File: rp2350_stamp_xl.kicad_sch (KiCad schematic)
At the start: 47 parts, among them J1 Conn_North, J2 Conn_West, J3 Conn_East, J4 Conn_South, J5 Conn_Pi_SWD, J6 Conn_Pi_UART, Q1 BSS84, SW1 SW_RESET, SW2 SW_BOOTSEL, U1 W25Q128JVPIQ, U2 ME4055, U3 AP2112K-3.3, U4 FLASH or PSRAM, U5 RP235x-B, Y1 XYDBPCNANF-12MHZ

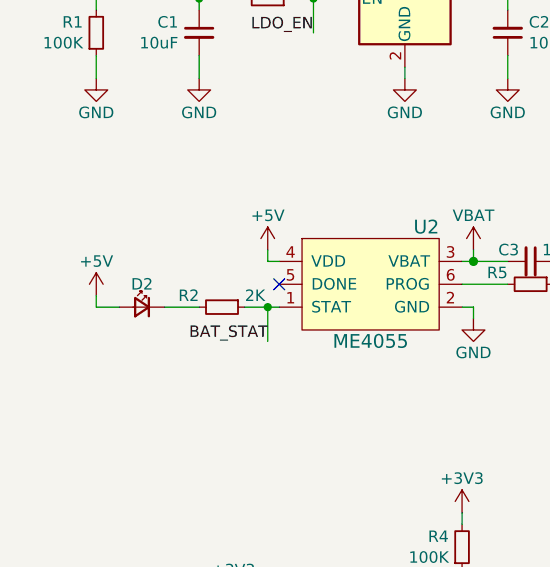
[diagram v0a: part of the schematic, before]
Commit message: Rev 3
- Rev 2 added logo and QR Code
- Put chip name on the board
- Fixup pin markers to be uniform
- Add battery icon
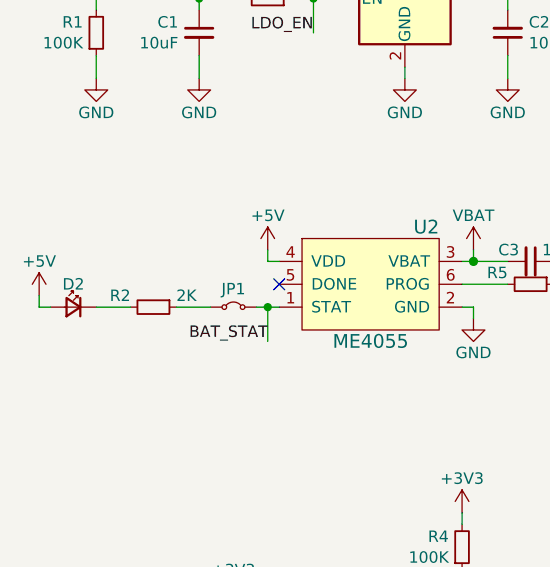
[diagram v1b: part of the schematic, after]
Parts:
- added JP1: SJ_STAT_LED, Jumper:SolderJumper-2_P1.3mm_Bridged_RoundedPad1.0x1.5mm, symbol Jumper:Jumper_2_Small_Bridged
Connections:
- net BAT_STAT: now also JP1.2 (B); no longer R2.1
- new net: JP1.1 (A), R2.1
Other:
- moved on the sheet: D2, R2
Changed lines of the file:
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@@
 	(wire
 		(pts
+			(xy 44.45 96.52) (xy 45.72 96.52)
+		)
+		(stroke
+			(width 0)
+			(type default)
+		)
+	)
+	(wire
+		(pts
 			(xy 41.91 180.34) (xy 41.91 181.61)
 		)
@@
 	(wire
 		(pts
-			(xy 26.67 96.52) (xy 29.21 96.52)
+			(xy 20.32 96.52) (xy 21.59 96.52)
 		)
 		(stroke
@@
 	(wire
 		(pts
-			(xy 45.72 96.52) (xy 43.18 96.52)
-		)
-		(stroke
-			(width 0)
-			(type solid)
-		)
-	)
-	(wire
-		(pts
 			(xy 135.89 77.47) (xy 142.24 77.47)
 		)
@@
 	(wire
 		(pts
-			(xy 38.1 96.52) (xy 34.29 96.52)
+			(xy 30.48 96.52) (xy 26.67 96.52)
 		)
 		(stroke
@@
 	(wire
 		(pts
-			(xy 26.67 96.52) (xy 26.67 95.25)
+			(xy 20.32 96.52) (xy 20.32 95.25)
 		)
 		(stroke
@@
 	(wire
 		(pts
+			(xy 35.56 96.52) (xy 39.37 96.52)
+		)
+		(stroke
+			(width 0)
+			(type default)
+		)
+	)
+	(wire
+		(pts
 			(xy 205.74 90.17) (xy 204.47 90.17)
 		)
@@
 	)
 	(symbol
+		(lib_id "Jumper:Jumper_2_Small_Bridged")
+		(at 41.91 96.52 0)
+		(unit 1)
+		(exclude_from_sim yes)
+		(in_bom no)
+		(on_board yes)
+		(dnp no)
+		(property "Reference" "JP1"
+			(at 41.91 95.25 0)
+			(effects
+				(font
+					(size 1.27 1.27)
+				)
+				(justify bottom)
+			)
+		)
+		(property "Value" "SJ_STAT_LED"
+			(at 41.91 97.79 0)
+			(effects
+				(font
+					(size 1.27 1.27)
+				)
+				(justify top)
+				(hide yes)
+			)
+		)
+		(property "Footprint" "Jumper:SolderJumper-2_P1.3mm_Bridged_RoundedPad1.0x1.5mm"
+			(at 41.91 96.52 0)
+			(effects
+				(font
+					(size 1.27 1.27)
+				)
+				(hide yes)
+			)
+		)
+		(property "Datasheet" "~"
+			(at 41.91 96.52 0)
+			(effects
+				(font
+					(size 1.27 1.27)
+				)
+				(hide yes)
+			)
+		)
+		(property "Description" "Jumper, 2-pole, small symbol, bridged"
+			(at 41.91 96.52 0)
+			(effects
+				(font
+					(size 1.27 1.27)
+				)
+				(hide yes)
+			)
+		)
+		(pin "1"
+		)
+		(pin "2"
+		)
+		(instances
+			(project "rp2350_stamp_xl"
+				(path "/019f2816-6bfb-4531-95b3-45f73cf5fc4b"
+					(reference "JP1")
+					(unit 1)
+				)
+			)
+		)
+	)
+	(symbol
 		(lib_id "power:GND")
 		(at 60.96 71.12 0)
@@
 	(symbol
 		(lib_id "Device:R_Small")
-		(at 40.64 96.52 270)
+		(at 33.02 96.52 270)
 		(unit 1)
 		(exclude_from_sim no)
@@
 		(dnp no)
 		(property "Reference" "R2"
-			(at 38.1 95.25 90)
+			(at 30.48 95.25 90)
 			(effects
 				(font
@@
 		)
 		(property "Value" "2K"
-			(at 43.18 95.25 90)
+			(at 35.56 95.25 90)
 			(effects
 				(font
@@
 		)
 		(property "Footprint" "Resistor_SMD:R_0603_1608Metric"
-			(at 40.64 96.52 0)
+			(at 33.02 96.52 0)
 			(effects
 				(font
@@
 		)
 		(property "Datasheet" "~"
-			(at 40.64 96.52 0)
+			(at 33.02 96.52 0)
 			(effects
 				(font
@@
 		)
 		(property "Description" ""
-			(at 40.64 96.52 0)
+			(at 33.02 96.52 0)
 			(effects
 				(font
@@
 	(symbol
 		(lib_id "power:+5V")
-		(at 26.67 95.25 0)
+		(at 20.32 95.25 0)
 		(unit 1)
 		(exclude_from_sim no)
@@
 		(dnp no)
 		(property "Reference" "#PWR03"
-			(at 26.67 99.06 0)
+			(at 20.32 99.06 0)
 			(effects
 				(font
@@
 		)
 		(property "Value" "+5V"
-			(at 26.67 91.44 0)
+			(at 20.32 91.44 0)
 			(effects
 				(font
@@
 		)
 		(property "Footprint" ""
-			(at 26.67 95.25 0)
+			(at 20.32 95.25 0)
 			(effects
 				(font
@@
 		)
 		(property "Datasheet" ""
-			(at 26.67 95.25 0)
+			(at 20.32 95.25 0)
 			(effects
 				(font
@@
 		)
 		(property "Description" ""
-			(at 26.67 95.25 0)
+			(at 20.32 95.25 0)
 			(effects
 				(font
@@
 	(symbol
 		(lib_id "Device:LED_Small")
-		(at 31.75 96.52 0)
+		(at 24.13 96.52 0)
 		(mirror y)
 		(unit 1)
@@
 		(dnp no)
 		(property "Reference" "D2"
-			(at 31.75 93.98 0)
+			(at 24.13 93.98 0)
 			(effects
 				(font
@@
 		)
 		(property "Value" "LED_CHR"
-			(at 31.75 92.8624 0)
+			(at 24.13 92.8624 0)
 			(effects
 				(font
@@
 		)
 		(property "Footprint" "LED_SMD:LED_0603_1608Metric"
-			(at 31.75 96.52 90)
+			(at 24.13 96.52 90)
 			(effects
 				(font
@@
 		)
 		(property "Datasheet" "~"
-			(at 31.75 96.52 90)
+			(at 24.13 96.52 90)
 			(effects
 				(font
@@
 		)
 		(property "Description" ""
-			(at 31.75 96.52 0)
+			(at 24.13 96.52 0)
 			(effects
 				(font

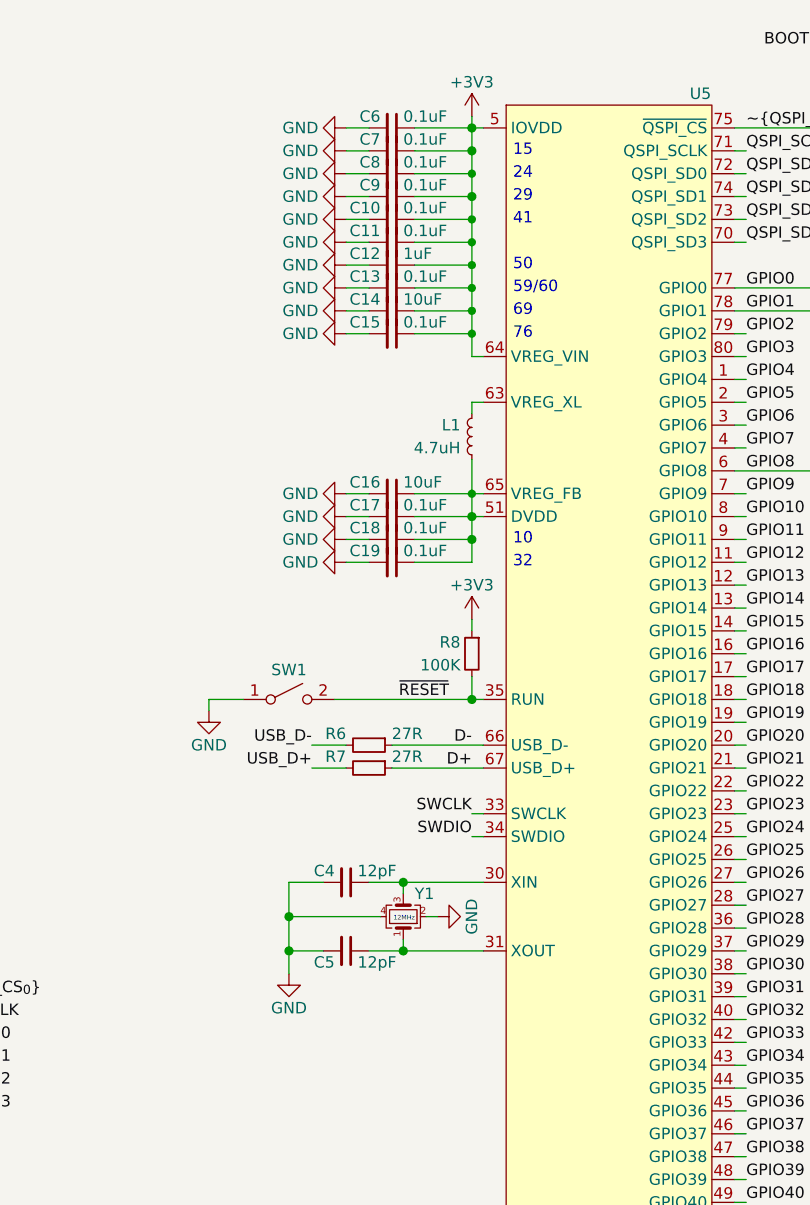
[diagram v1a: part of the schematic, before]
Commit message: Rev 3.5
Fixup power stuff according to RPi's recommendations
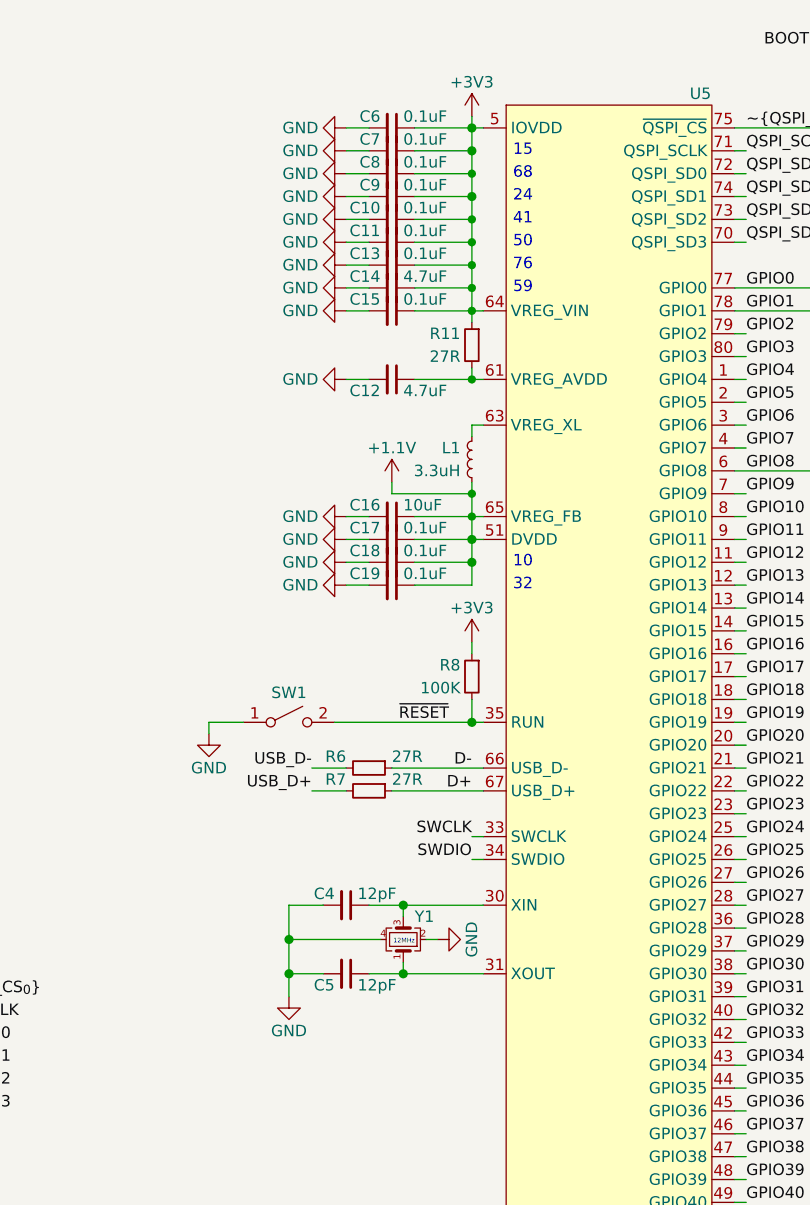
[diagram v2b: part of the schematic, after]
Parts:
- added R11: 27R, Resistor_SMD:R_0603_1608Metric, symbol Device:R_Small
- C12: value 1uF -> 4.7uF
- C14: value 10uF -> 4.7uF
- L1: value 4.7uH -> 3.3uH
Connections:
- net +3V3: now also R11.1; no longer C12.1, U5.61 (IOVDD)
- net +1.1V: now reaches C16.1, C17.1, C18.1, C19.1, L1.1, U5.10 (DVDD), U5.32 (DVDD), U5.51 (DVDD), U5.65 (VREG_FB)
- new net: C12.1, R11.2, U5.61 (VREG_AVDD)
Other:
- note added: "59"
- note added: "68"
- note removed: "29"
- note removed: "59/60"
- note removed: "69"
- moved on the sheet: C12, C13, C14, C15, C16, C17, C18, C19, C4, C5, L1, R6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

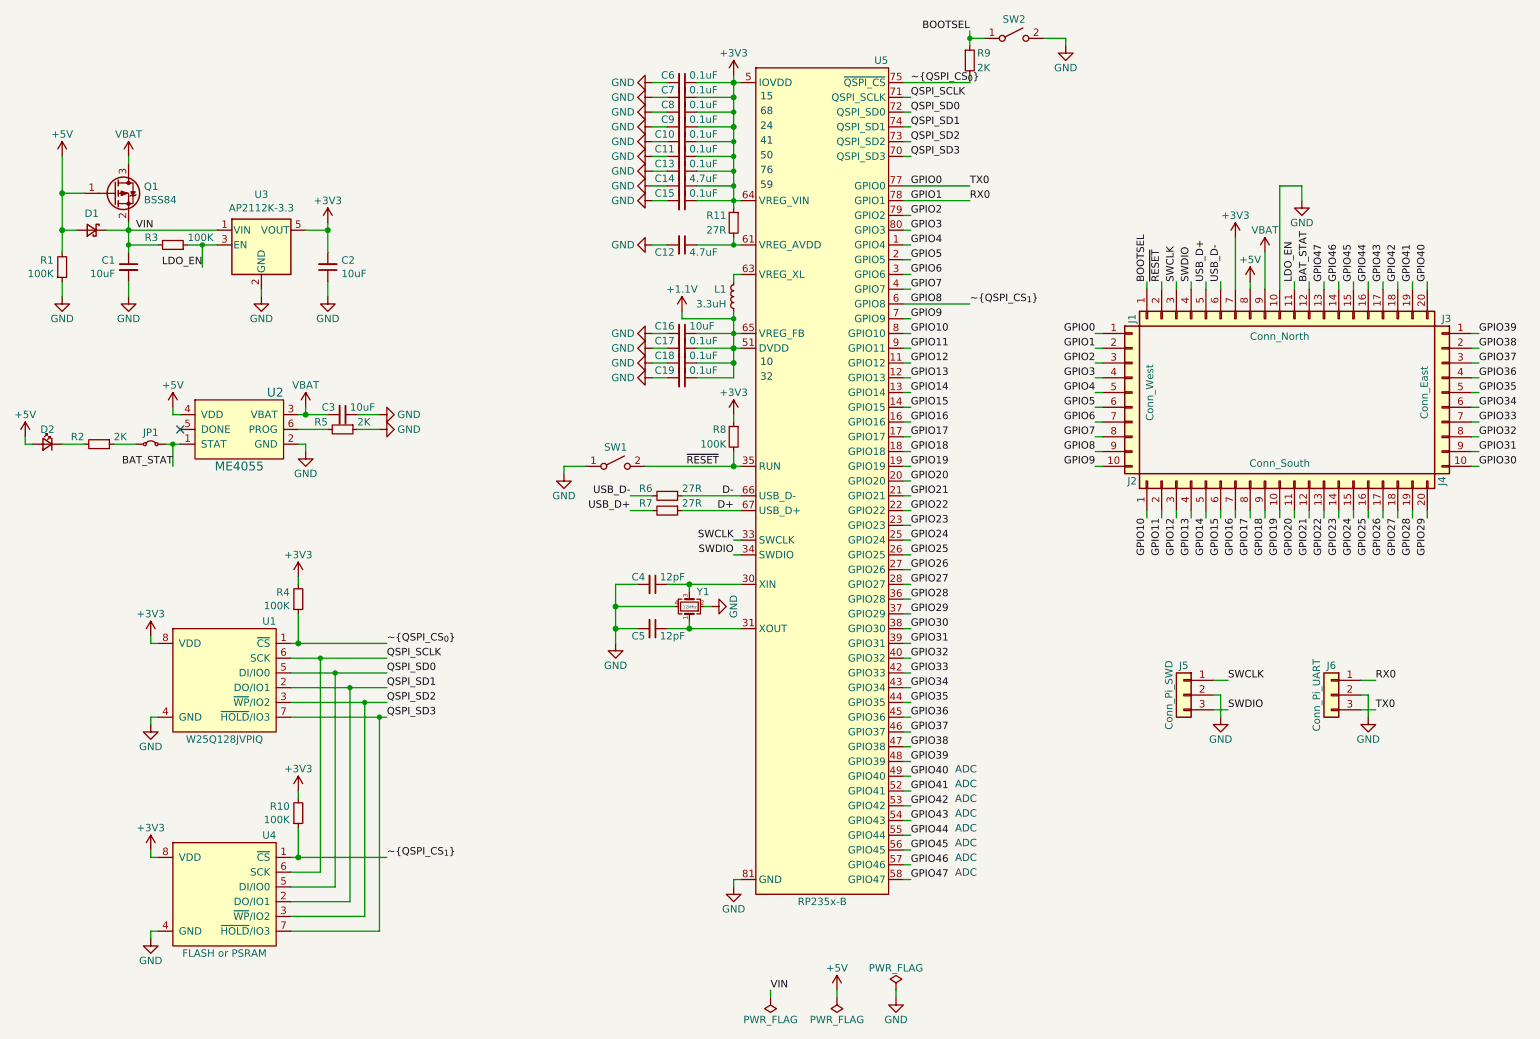
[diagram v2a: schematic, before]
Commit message: Fix BOM info, add README and LICENSE
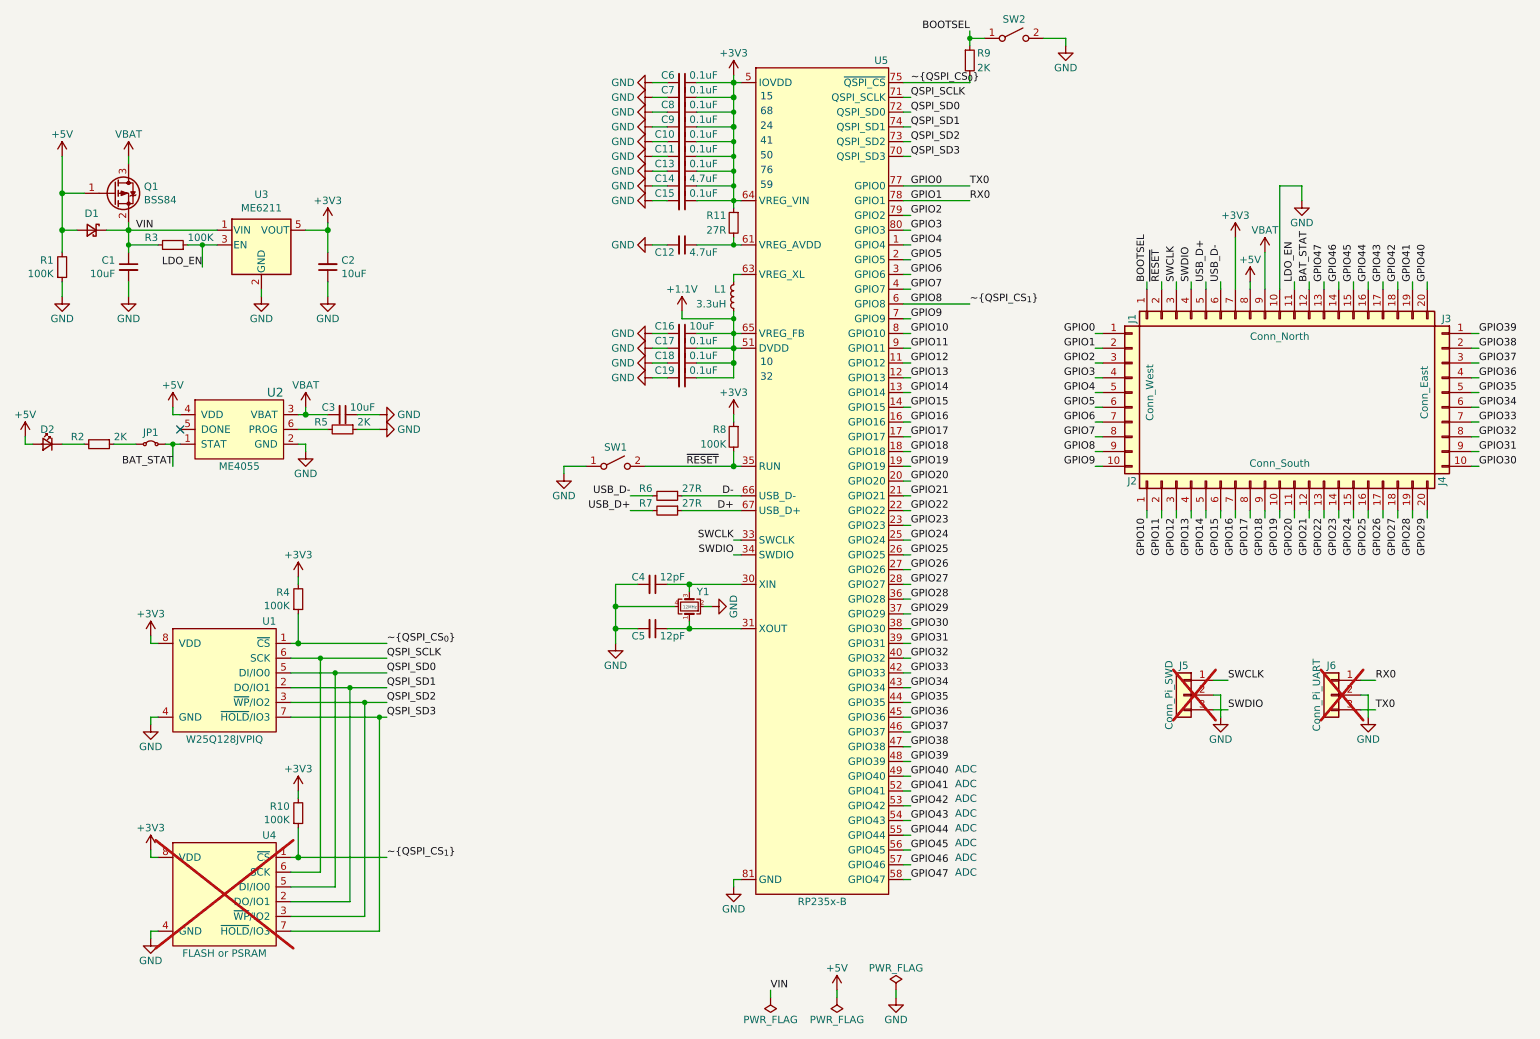
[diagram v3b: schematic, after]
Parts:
- J1, J2, J3, J4: now left out of the parts list
- J5, J6, U4: now not fitted
- L1: LCSC C5349608 -> C5832359
- SW1, SW2: LCSC (none) -> C561514
- U3: value AP2112K-3.3 -> ME6211; Digikey AP2112K-3.3TRG1DICT-ND -> (none); LCSC C51118 -> C82942
- Y1: value XYDBPCNANF-12MHZ -> CM4012M00012001; LCSC C521567 -> C7294611
